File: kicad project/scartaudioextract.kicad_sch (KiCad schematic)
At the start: 3 parts, among them J1 SCART-F, J2 SCART-F, J3 AudioJack3

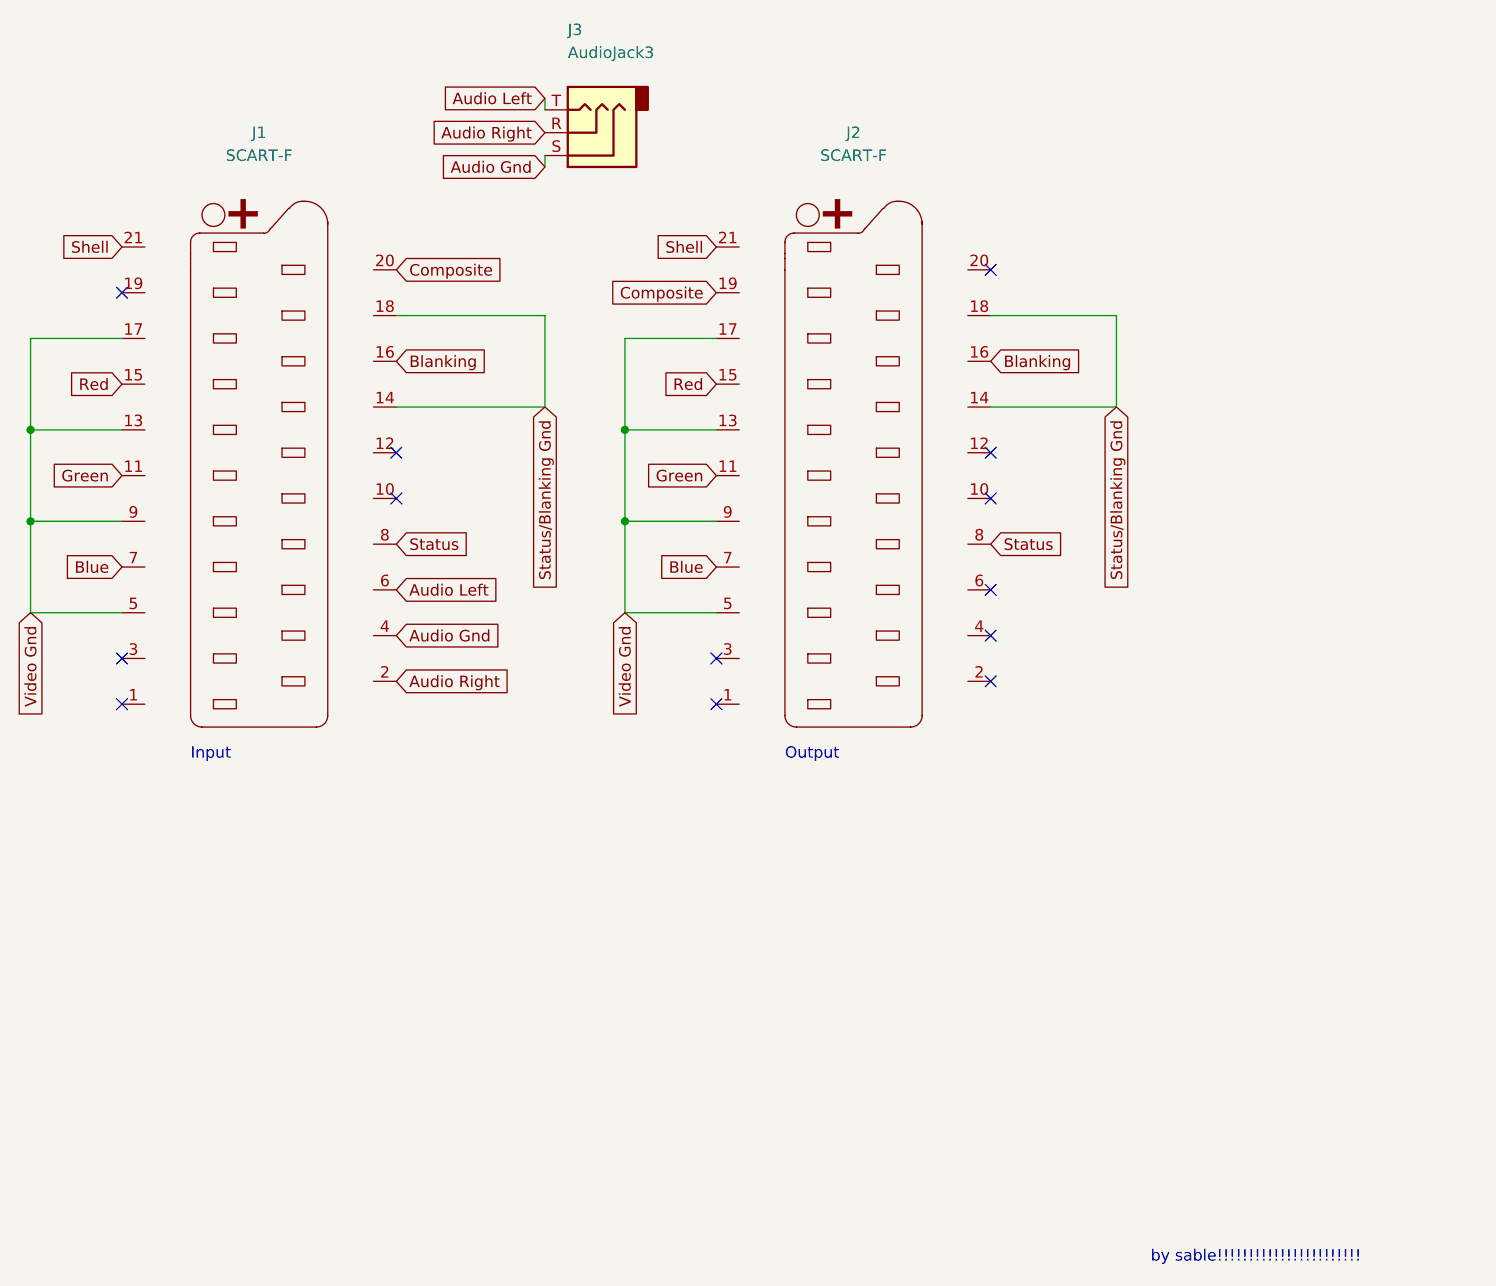
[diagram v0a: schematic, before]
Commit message: add termination resistors
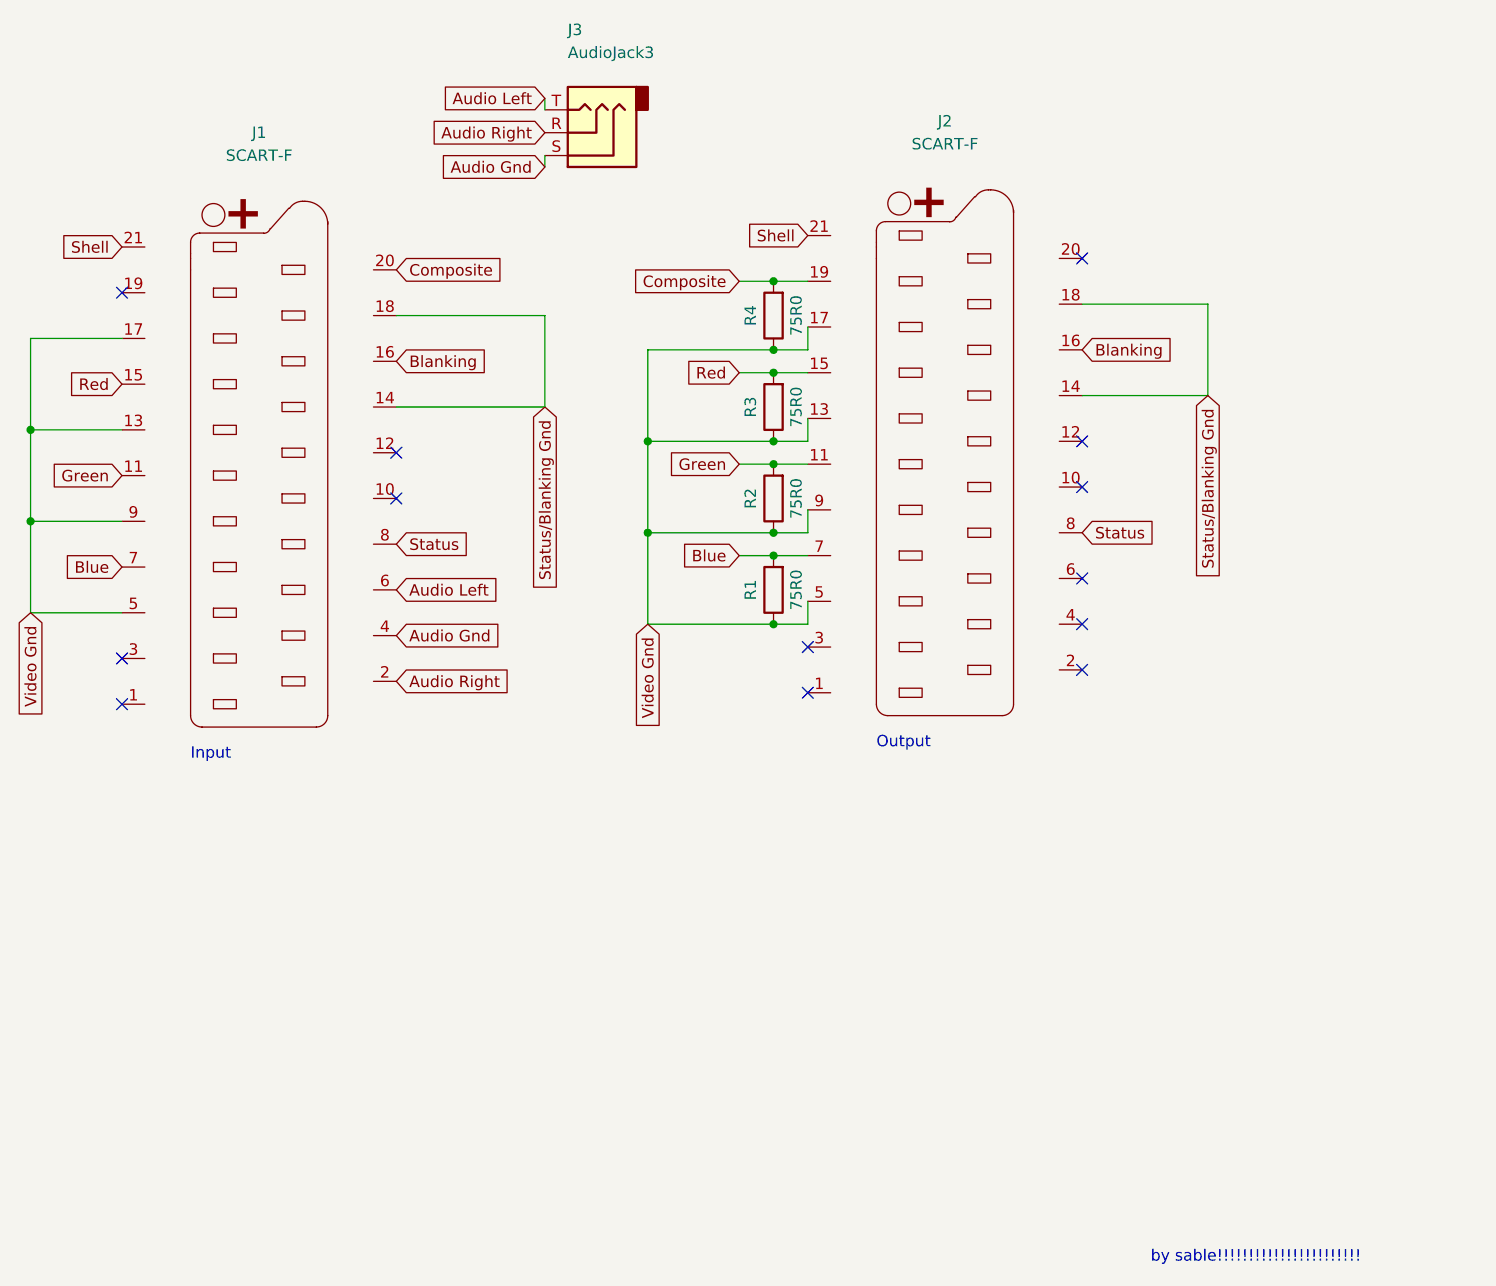
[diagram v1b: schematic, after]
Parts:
- added R1, R2, R3, R4: 75R0, Resistor_SMD:R_0805_2012Metric_Pad1.20x1.40mm_HandSolder, symbol Device:R
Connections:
- net Blue: now also R1.2
- net Composite: now also R4.2
- net Green: now also R2.2
- net Red: now also R3.2
- net Video Gnd: now also R1.1, R2.1, R3.1, R4.1
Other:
- moved on the sheet: J2

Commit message: remove termination resistors
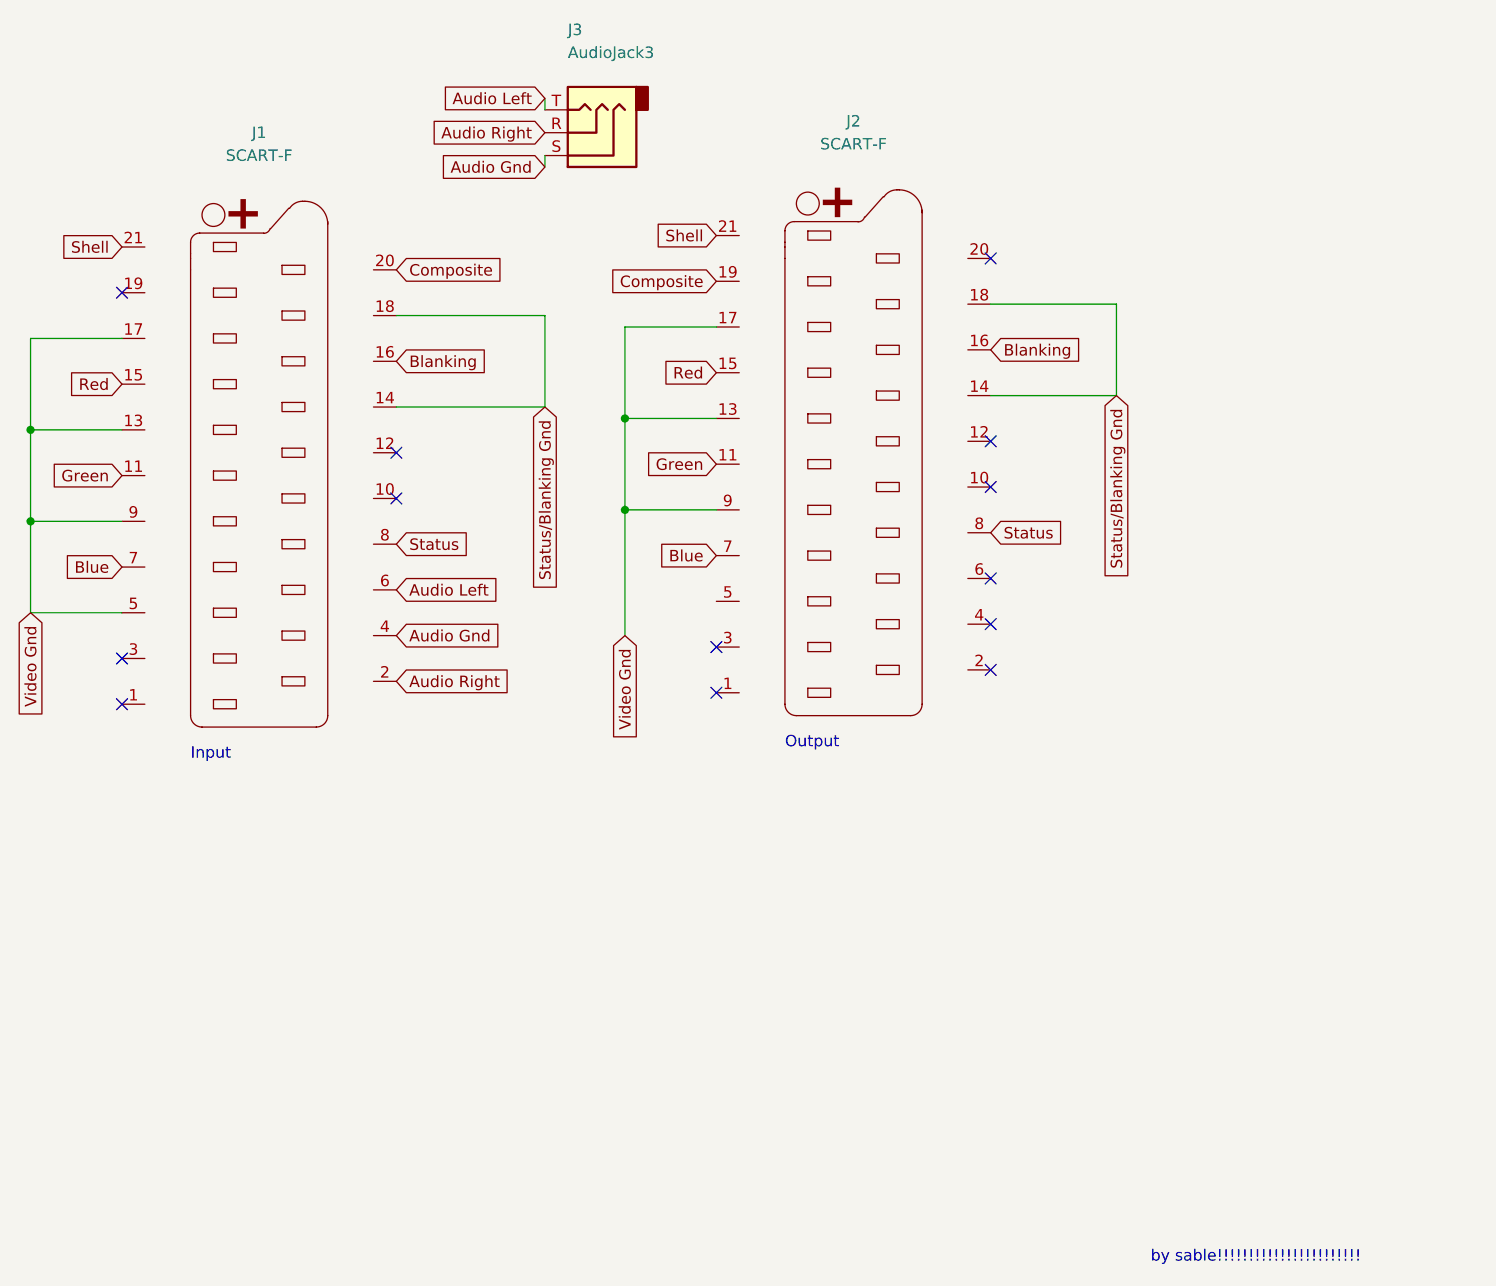
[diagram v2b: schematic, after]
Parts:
- removed R1, R2, R3, R4: 75R0, Resistor_SMD:R_0805_2012Metric_Pad1.20x1.40mm_HandSolder, symbol Device:R
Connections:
- net Video Gnd: no longer J2.5 (P5)
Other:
- moved on the sheet: J2

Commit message: forgot a connection
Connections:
- net Video Gnd: now also J2.5 (P5)
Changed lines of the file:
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@@
   (junction (at 58.42 91.44) (diameter 0) (color 0 0 0 0)
+  )
+  (junction (at 124.46 100.33) (diameter 0) (color 0 0 0 0)
   )
   (junction (at 124.46 90.17) (diameter 0) (color 0 0 0 0)
@@
     (stroke (width 0) (type default))
   )
+  (wire (pts (xy 124.46 100.33) (xy 124.46 104.14))
+    (stroke (width 0) (type default))
+  )
   (wire (pts (xy 115.57 68.58) (xy 115.57 78.74))
     (stroke (width 0) (type default))
@@
   )
   (wire (pts (xy 124.46 80.01) (xy 134.62 80.01))
+    (stroke (width 0) (type default))
+  )
+  (wire (pts (xy 124.46 100.33) (xy 134.62 100.33))
     (stroke (width 0) (type default))
   )
@@
     (stroke (width 0) (type default))
   )
-  (wire (pts (xy 124.46 90.17) (xy 124.46 104.14))
+  (wire (pts (xy 124.46 90.17) (xy 124.46 100.33))
     (stroke (width 0) (type default))
   )

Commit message: add extra info
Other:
- note added: "Impedance matching is not needed, the impedance is dealt with at the terminations"
- note added: "Take input from the input pins on the pinout only"
- note added: "Termination is only done in series at the transmitter, and in parallel to ground at the reciever"
- note added: "http://fr.meric.free.fr/Articles/articlesba/stsurtvplat/Scart/BS_EN_50049-1%20Peritelevision%20connector.pdf"
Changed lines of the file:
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@@
     (stroke (width 0) (type default))
+  )
+  (text "Take input from the input pins on the pinout only" (at 76.2 133.35 0)
+    (effects (font (size 1.27 1.27)) (justify left bottom))
+  )
+  (text "Termination is only done in series at the transmitter, and in parallel to ground at the reciever"
+    (at 76.2 138.43 0)
+    (effects (font (size 1.27 1.27)) (justify left bottom))
   )
   (text "Input" (at 76.2 118.11 0)
@@
     (effects (font (size 1.27 1.27)) (justify left bottom))
   )
+  (text "http://fr.meric.free.fr/Articles/articlesba/stsurtvplat/Scart/BS_EN_50049-1%20Peritelevision%20connector.pdf"
+    (at 76.2 140.97 0)
+    (effects (font (size 1.27 1.27)) (justify left bottom))
+  )
+  (text "Impedance matching is not needed, the impedance is dealt with at the terminations"
+    (at 76.2 135.89 0)
+    (effects (font (size 1.27 1.27)) (justify left bottom))
+  )

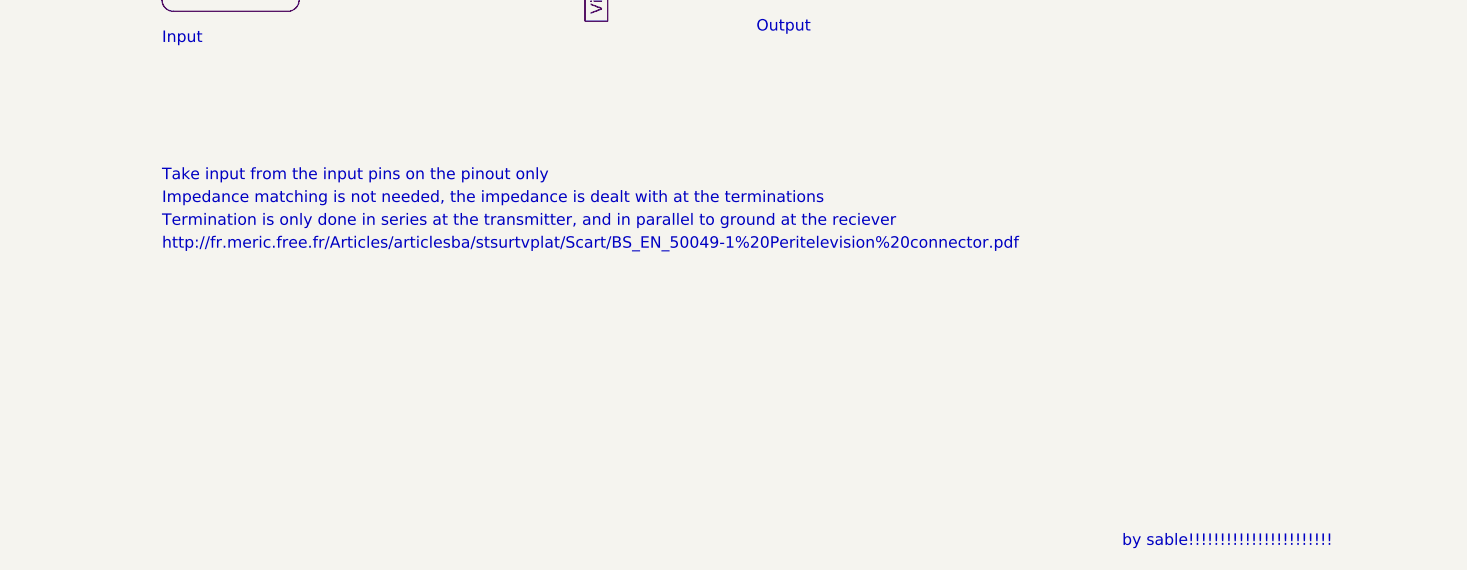
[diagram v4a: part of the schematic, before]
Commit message: improve schematic, use better design rules
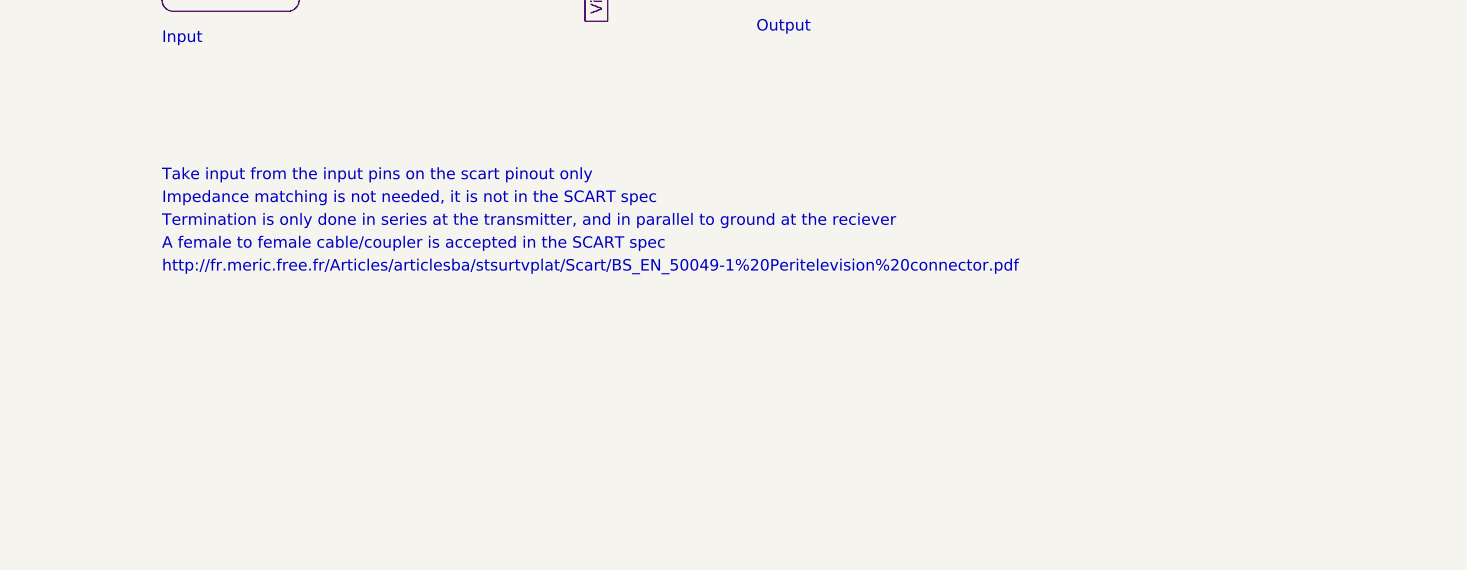
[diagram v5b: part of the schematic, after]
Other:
- note added: "A female to female cable/coupler is accepted in the SCART spec"
- note added: "Impedance matching is not needed, it is not in the SCART spec"
- note added: "Take input from the input pins on the scart pinout only"
- note removed: "Impedance matching is not needed, the impedance is dealt with at the terminations"
- note removed: "Take input from the input pins on the pinout only"
- note removed: "by sable!!!!!!!!!!!!!!!!!!!!!!!"
- title: (none) -> Scart Audio Extractor
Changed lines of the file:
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@@
 (kicad_sch (version 20230121) (generator eeschema)
   (paper "A4")
+  (title_block
+    (title "Scart Audio Extractor")
+    (date "8/25/2024")
+    (rev "1.2")
+    (comment 1 "made by sable!!!!!!!!!!!!!!!!!!!!!!!")
+  )
   (junction (at 124.46 80.01) (diameter 0) (color 0 0 0 0)
   )
@@
     (stroke (width 0) (type default))
   )
-  (text "Take input from the input pins on the pinout only" (at 76.2 133.35 0)
+  (text "Take input from the input pins on the scart pinout only"
+    (at 76.2 133.35 0)
     (effects (font (size 1.27 1.27)) (justify left bottom))
   )
@@
     (effects (font (size 1.27 1.27)) (justify left bottom))
   )
-  (text "by sable!!!!!!!!!!!!!!!!!!!!!!!" (at 182.88 173.99 0)
+  (text "http://fr.meric.free.fr/Articles/articlesba/stsurtvplat/Scart/BS_EN_50049-1%20Peritelevision%20connector.pdf"
+    (at 76.2 143.51 0)
     (effects (font (size 1.27 1.27)) (justify left bottom))
   )
-  (text "http://fr.meric.free.fr/Articles/articlesba/stsurtvplat/Scart/BS_EN_50049-1%20Peritelevision%20connector.pdf"
+  (text "Impedance matching is not needed, it is not in the SCART spec"
+    (at 76.2 135.89 0)
+    (effects (font (size 1.27 1.27)) (justify left bottom))
+  )
+  (text "A female to female cable/coupler is accepted in the SCART spec\n"
     (at 76.2 140.97 0)
     (effects (font (size 1.27 1.27)) (justify left bottom))
   )
-  (text "Impedance matching is not needed, the impedance is dealt with at the terminations"
-    (at 76.2 135.89 0)
-    (effects (font (size 1.27 1.27)) (justify left bottom))
-  )
